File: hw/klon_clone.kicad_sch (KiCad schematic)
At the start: 74 parts

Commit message: Annotated sch.
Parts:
- gave numbers to parts that had none: 70

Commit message: Added all footprints but switch footprint.
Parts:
- C1, C7: footprint (none) -> Capacitor_THT:C_Rect_L13.0mm_W5.0mm_P10.00mm_FKS3_FKP3_MKS4
- C13: footprint (none) -> Capacitor_THT:C_Rect_L10.3mm_W5.0mm_P7.50mm_MKS4
- C14: footprint (none) -> Capacitor_THT:C_Rect_L10.0mm_W4.0mm_P7.50mm_MKS4
- C16, C6: footprint (none) -> Capacitor_THT:CP_Radial_D8.0mm_P5.00mm
- C18: footprint (none) -> Capacitor_THT:C_Rect_L18.0mm_W7.0mm_P15.00mm_FKS3_FKP3
- C19: footprint (none) -> Capacitor_THT:C_Rect_L10.3mm_W4.5mm_P7.50mm_MKS4
- C20: footprint (none) -> Capacitor_THT:C_Rect_L13.0mm_W4.0mm_P10.00mm_FKS3_FKP3_MKS4
- C21: footprint (none) -> Capacitor_THT:C_Rect_L16.5mm_W5.0mm_P15.00mm_MKT
- C22, C5: footprint (none) -> Capacitor_THT:CP_Radial_D5.0mm_P2.00mm
- C3: footprint (none) -> Capacitor_THT:C_Axial_L19.0mm_D9.5mm_P25.00mm_Horizontal
- C4, C9: footprint (none) -> Capacitor_THT:C_Axial_L5.1mm_D3.1mm_P15.00mm_Horizontal
- D4: footprint (none) -> LED_THT:LED_D5.0mm
- D5, D6: footprint (none) -> Diode_THT:D_DO-35_SOD27_P10.16mm_Horizontal
- J1, J3, RV1, RV2, RV3, RV4: footprint (none) -> Connector_PinHeader_2.54mm:PinHeader_1x03_P2.54mm_Vertical
- J2: footprint (none) -> Connector_PinHeader_2.54mm:PinHeader_1x02_P2.54mm_Vertical
- R1, R10, R11, R12, R13, R14, R15, R16, R17, R18, R19, R2, R20, R21, R22, R23, R24, R25, R26, R27, R28, R29, R3, R30, R4, R5, R6, R7, R8, R9: footprint (none) -> Resistor_THT:R_Axial_DIN0207_L6.3mm_D2.5mm_P15.24mm_Horizontal
- SW1, SW2: footprint (none) -> Connector_PinHeader_2.54mm:PinHeader_1x06_P2.54mm_Vertical

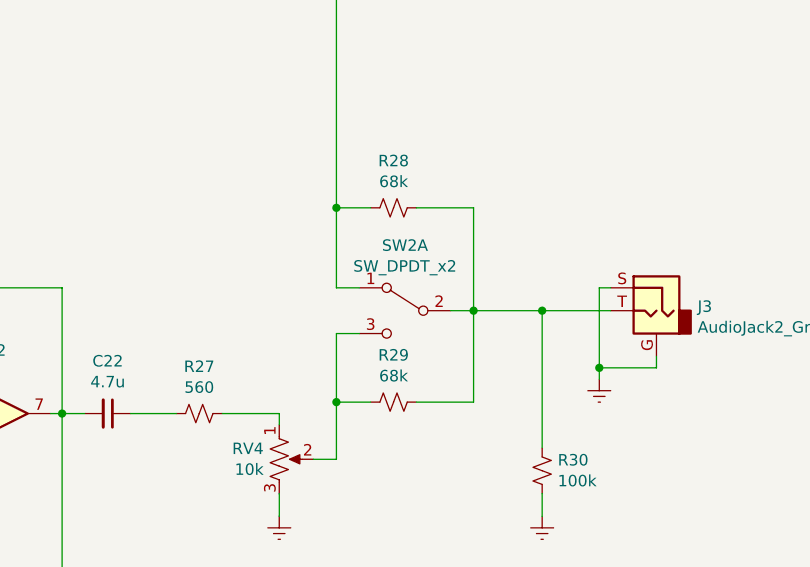
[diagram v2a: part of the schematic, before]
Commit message: Added SOIC Opamp footprints.
Added tenative footprints for opamps. Double check we have right package. Need to add footprint for Power supply IC>
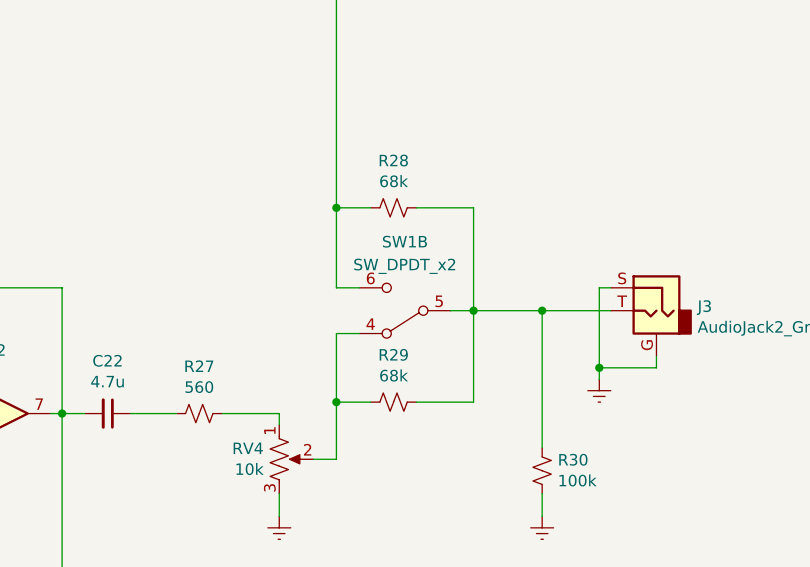
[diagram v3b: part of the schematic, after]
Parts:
- removed SW2: SW_DPDT_x2, Connector_PinHeader_2.54mm:PinHeader_1x06_P2.54mm_Vertical, symbol Switch:SW_DPDT_x2
- added unit 2 of SW1
- U1, U3: footprint (none) -> Package_SO:SO-8_5.3x6.2mm_P1.27mm
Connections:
- net at R29.2, RV4.2: now also SW1.4 (A)
- net at R28.2, R7.1: now also SW1.6 (C)
- net at J3.T, R28.1, R29.1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: now also SW1.5 (B)
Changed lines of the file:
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@@
     (property "Reference" "U1" (id 0) (at 87.63 71.9582 0))
     (property "Value" "TL072" (id 1) (at 87.63 74.2696 0))
-    (property "Footprint" "" (id 2) (at 87.63 81.28 0)
+    (property "Footprint" "Package_SO:SO-8_5.3x6.2mm_P1.27mm" (id 2) (at 87.63 81.28 0)
       (effects (font (size 1.27 1.27)) hide)
     )
@@
     (property "Reference" "U1" (id 0) (at 173.99 74.4982 0))
     (property "Value" "TL072" (id 1) (at 173.99 76.8096 0))
-    (property "Footprint" "" (id 2) (at 173.99 83.82 0)
+    (property "Footprint" "Package_SO:SO-8_5.3x6.2mm_P1.27mm" (id 2) (at 173.99 83.82 0)
       (effects (font (size 1.27 1.27)) hide)
     )
@@
     (property "Reference" "U3" (id 0) (at 279.4 77.0382 0))
     (property "Value" "TL072" (id 1) (at 279.4 79.3496 0))
-    (property "Footprint" "" (id 2) (at 279.4 86.36 0)
+    (property "Footprint" "Package_SO:SO-8_5.3x6.2mm_P1.27mm" (id 2) (at 279.4 86.36 0)
       (effects (font (size 1.27 1.27)) hide)
     )
@@
     (property "Reference" "U3" (id 0) (at 318.77 79.5782 0))
     (property "Value" "TL072" (id 1) (at 318.77 81.8896 0))
-    (property "Footprint" "" (id 2) (at 318.77 88.9 0)
+    (property "Footprint" "Package_SO:SO-8_5.3x6.2mm_P1.27mm" (id 2) (at 318.77 88.9 0)
       (effects (font (size 1.27 1.27)) hide)
     )
@@
     )
     (property "Datasheet" "~" (id 3) (at 351.79 93.98 0)
-      (effects (font (size 1.27 1.27)) hide)
-    )
-    (pin "1")
-    (pin "2")
-    (pin "3")
-  )
-  (symbol (lib_id "Switch:SW_DPDT_x2") (at 365.76 77.47 0) (mirror y) (unit 1)
-    (in_bom yes) (on_board yes)
-    (property "Reference" "SW2" (id 0) (at 365.76 70.231 0))
-    (property "Value" "SW_DPDT_x2" (id 1) (at 365.76 72.5424 0))
-    (property "Footprint" "Connector_PinHeader_2.54mm:PinHeader_1x06_P2.54mm_Vertical" (id 2) (at 365.76 77.47 0)
-      (effects (font (size 1.27 1.27)) hide)
-    )
-    (property "Datasheet" "~" (id 3) (at 365.76 77.47 0)
       (effects (font (size 1.27 1.27)) hide)
     )
@@
       (effects (font (size 1.27 1.27)) (justify left))
     )
-    (property "Footprint" "" (id 2) (at 87.63 81.28 0)
+    (property "Footprint" "Package_SO:SO-8_5.3x6.2mm_P1.27mm" (id 2) (at 87.63 81.28 0)
       (effects (font (size 1.27 1.27)) hide)
     )
@@
       (effects (font (size 1.27 1.27)) (justify left))
     )
-    (property "Footprint" "" (id 2) (at 279.4 86.36 0)
+    (property "Footprint" "Package_SO:SO-8_5.3x6.2mm_P1.27mm" (id 2) (at 279.4 86.36 0)
       (effects (font (size 1.27 1.27)) hide)
     )
@@
     )
     (pin "1")
+  )
+  (symbol (lib_id "Switch:SW_DPDT_x2") (at 365.76 77.47 180) (unit 2)
+    (in_bom yes) (on_board yes) (fields_autoplaced)
+    (property "Reference" "SW1" (id 0) (at 365.76 69.85 0))
+    (property "Value" "SW_DPDT_x2" (id 1) (at 365.76 72.39 0))
+    (property "Footprint" "Connector_PinHeader_2.54mm:PinHeader_1x06_P2.54mm_Vertical" (id 2) (at 365.76 77.47 0)
+      (effects (font (size 1.27 1.27)) hide)
+    )
+    (property "Datasheet" "~" (id 3) (at 365.76 77.47 0)
+      (effects (font (size 1.27 1.27)) hide)
+    )
+    (pin "4")
+    (pin "5")
+    (pin "6")
   )
   (sheet_instances
@@
       (reference "SW1") (unit 1) (value "SW_DPDT_x2") (footprint "Connector_PinHeader_2.54mm:PinHeader_1x06_P2.54mm_Vertical")
     )
-    (path "/00000000-0000-0000-0000-000061c3b78a"
-      (reference "SW2") (unit 1) (value "SW_DPDT_x2") (footprint "Connector_PinHeader_2.54mm:PinHeader_1x06_P2.54mm_Vertical")
+    (path "/a1c80773-df7f-4f73-ae79-2de08d81dd4b"
+      (reference "SW1") (unit 2) (value "SW_DPDT_x2") (footprint "Connector_PinHeader_2.54mm:PinHeader_1x06_P2.54mm_Vertical")
     )
     (path "/00000000-0000-0000-0000-000061c0f078"
-      (reference "U1") (unit 1) (value "TL072") (footprint "")
+      (reference "U1") (unit 1) (value "TL072") (footprint "Package_SO:SO-8_5.3x6.2mm_P1.27mm")
     )
     (path "/00000000-0000-0000-0000-000061c176e6"
-      (reference "U1") (unit 2) (value "TL072") (footprint "")
+      (reference "U1") (unit 2) (value "TL072") (footprint "Package_SO:SO-8_5.3x6.2mm_P1.27mm")
     )
     (path "/00000000-0000-0000-0000-000061c5b223"
-      (reference "U1") (unit 3) (value "TL072") (footprint "")
+      (reference "U1") (unit 3) (value "TL072") (footprint "Package_SO:SO-8_5.3x6.2mm_P1.27mm")
     )
     (path "/00000000-0000-0000-0000-000061c4201c"
@@
     )
     (path "/00000000-0000-0000-0000-000061c29fb1"
-      (reference "U3") (unit 1) (value "TL072") (footprint "")
+      (reference "U3") (unit 1) (value "TL072") (footprint "Package_SO:SO-8_5.3x6.2mm_P1.27mm")
     )
     (path "/00000000-0000-0000-0000-000061c35021"
-      (reference "U3") (unit 2) (value "TL072") (footprint "")
+      (reference "U3") (unit 2) (value "TL072") (footprint "Package_SO:SO-8_5.3x6.2mm_P1.27mm")
     )
     (path "/00000000-0000-0000-0000-000061c5fbc0"
-      (reference "U3") (unit 3) (value "TL072") (footprint "")
-    )
-  )
+      (reference "U3") (unit 3) (value "TL072") (footprint "Package_SO:SO-8_5.3x6.2mm_P1.27mm")
+    )
+  )

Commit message: Assigned SO8 to ICL7660
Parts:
- U2: footprint (none) -> Package_SO:SO-8_5.3x6.2mm_P1.27mm
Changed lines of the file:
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@@
     (property "Reference" "U2" (id 0) (at 168.91 192.6082 0))
     (property "Value" "ICL7660" (id 1) (at 168.91 194.9196 0))
-    (property "Footprint" "" (id 2) (at 166.37 209.55 0)
+    (property "Footprint" "Package_SO:SO-8_5.3x6.2mm_P1.27mm" (id 2) (at 166.37 209.55 0)
       (effects (font (size 1.27 1.27)) hide)
     )
@@
     )
     (path "/00000000-0000-0000-0000-000061c4201c"
-      (reference "U2") (unit 1) (value "ICL7660") (footprint "")
+      (reference "U2") (unit 1) (value "ICL7660") (footprint "Package_SO:SO-8_5.3x6.2mm_P1.27mm")
     )
     (path "/00000000-0000-0000-0000-000061c29fb1"

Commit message: Assigned new cap footprint for 1uF
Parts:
- C10, C11, C12, C15, C17, C2, C8: footprint (none) -> kicad_footprint_library:C_Axial_L17.5mm_W7.8mm_P7.5mm_Horizontal
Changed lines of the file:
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@@
     (property "Reference" "C15" (id 0) (at 189.23 78.0034 90))
     (property "Value" "1u" (id 1) (at 189.23 80.3148 90))
-    (property "Footprint" "" (id 2) (at 189.23 83.82 0)
+    (property "Footprint" "kicad_footprint_library:C_Axial_L17.5mm_W7.8mm_P7.5mm_Horizontal" (id 2) (at 189.23 83.82 0)
       (effects (font (size 1.27 1.27)) hide)
     )
@@
       (effects (font (size 1.27 1.27)) (justify left))
     )
-    (property "Footprint" "" (id 2) (at 147.32 57.15 0)
+    (property "Footprint" "kicad_footprint_library:C_Axial_L17.5mm_W7.8mm_P7.5mm_Horizontal" (id 2) (at 147.32 57.15 0)
       (effects (font (size 1.27 1.27)) hide)
     )
@@
     (property "Reference" "C17" (id 0) (at 224.79 78.0034 90))
     (property "Value" "1u" (id 1) (at 224.79 80.3148 90))
-    (property "Footprint" "" (id 2) (at 224.79 83.82 0)
+    (property "Footprint" "kicad_footprint_library:C_Axial_L17.5mm_W7.8mm_P7.5mm_Horizontal" (id 2) (at 224.79 83.82 0)
       (effects (font (size 1.27 1.27)) hide)
     )
@@
       (effects (font (size 1.27 1.27)) (justify left))
     )
-    (property "Footprint" "" (id 2) (at 153.67 209.55 0)
+    (property "Footprint" "kicad_footprint_library:C_Axial_L17.5mm_W7.8mm_P7.5mm_Horizontal" (id 2) (at 153.67 209.55 0)
       (effects (font (size 1.27 1.27)) hide)
     )
@@
       (effects (font (size 1.27 1.27)) (justify left))
     )
-    (property "Footprint" "" (id 2) (at 110.49 205.74 0)
+    (property "Footprint" "kicad_footprint_library:C_Axial_L17.5mm_W7.8mm_P7.5mm_Horizontal" (id 2) (at 110.49 205.74 0)
       (effects (font (size 1.27 1.27)) hide)
     )
@@
       (effects (font (size 1.27 1.27)) (justify left))
     )
-    (property "Footprint" "" (id 2) (at 143.51 209.55 0)
+    (property "Footprint" "kicad_footprint_library:C_Axial_L17.5mm_W7.8mm_P7.5mm_Horizontal" (id 2) (at 143.51 209.55 0)
       (effects (font (size 1.27 1.27)) hide)
     )
@@
     (property "Reference" "C8" (id 0) (at 130.81 198.6534 90))
     (property "Value" "1u" (id 1) (at 130.81 200.9648 90))
-    (property "Footprint" "" (id 2) (at 130.81 204.47 0)
+    (property "Footprint" "kicad_footprint_library:C_Axial_L17.5mm_W7.8mm_P7.5mm_Horizontal" (id 2) (at 130.81 204.47 0)
       (effects (font (size 1.27 1.27)) hide)
     )
@@
     )
     (path "/00000000-0000-0000-0000-000061c48bfa"
-      (reference "C2") (unit 1) (value "1u") (footprint "")
+      (reference "C2") (unit 1) (value "1u") (footprint "kicad_footprint_library:C_Axial_L17.5mm_W7.8mm_P7.5mm_Horizontal")
     )
     (path "/00000000-0000-0000-0000-000061c22f5d"
@@
     )
     (path "/00000000-0000-0000-0000-000061c4d822"
-      (reference "C8") (unit 1) (value "1u") (footprint "")
+      (reference "C8") (unit 1) (value "1u") (footprint "kicad_footprint_library:C_Axial_L17.5mm_W7.8mm_P7.5mm_Horizontal")
     )
     (path "/00000000-0000-0000-0000-000061c1630a"
@@
     )
     (path "/00000000-0000-0000-0000-000061c4c2d3"
-      (reference "C10") (unit 1) (value "1u") (footprint "")
+      (reference "C10") (unit 1) (value "1u") (footprint "kicad_footprint_library:C_Axial_L17.5mm_W7.8mm_P7.5mm_Horizontal")
     )
     (path "/00000000-0000-0000-0000-000061c1ce7f"
-      (reference "C11") (unit 1) (value "1u") (footprint "")
+      (reference "C11") (unit 1) (value "1u") (footprint "kicad_footprint_library:C_Axial_L17.5mm_W7.8mm_P7.5mm_Horizontal")
     )
     (path "/00000000-0000-0000-0000-000061c46c41"
-      (reference "C12") (unit 1) (value "1u") (footprint "")
+      (reference "C12") (unit 1) (value "1u") (footprint "kicad_footprint_library:C_Axial_L17.5mm_W7.8mm_P7.5mm_Horizontal")
     )
     (path "/00000000-0000-0000-0000-000061c1b7dc"
@@
     )
     (path "/00000000-0000-0000-0000-000061c1c148"
-      (reference "C15") (unit 1) (value "1u") (footprint "")
+      (reference "C15") (unit 1) (value "1u") (footprint "kicad_footprint_library:C_Axial_L17.5mm_W7.8mm_P7.5mm_Horizontal")
     )
     (path "/00000000-0000-0000-0000-000061c4d184"
@@
     )
     (path "/00000000-0000-0000-0000-000061c21611"
-      (reference "C17") (unit 1) (value "1u") (footprint "")
+      (reference "C17") (unit 1) (value "1u") (footprint "kicad_footprint_library:C_Axial_L17.5mm_W7.8mm_P7.5mm_Horizontal")
     )
     (path "/00000000-0000-0000-0000-000061c2197d"

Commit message: Updated J1/J3 footprints and symbols. Initial layout placement.
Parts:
- removed J1, J3: AudioJack2_Ground, Connector_PinHeader_2.54mm:PinHeader_1x03_P2.54mm_Vertical, symbol Connector:AudioJack2_Ground
- added J1, J3: Conn_01x03_Male, Connector_PinHeader_2.54mm:PinHeader_1x03_P2.54mm_Vertical, symbol Connector:Conn_01x03_Male
- C10, C12, C2, C8: footprint kicad_footprint_library:C_Axial_L17.5mm_W7.8mm_P7.5mm_Horizontal -> Capacitor_SMD:C_0805_2012Metric_Pad1.18x1.45mm_HandSolder
- R1, R10, R11, R12, R13, R14, R15, R16, R17, R18, R19, R2, R20, R21, R22, R23, R24, R25, R26, R27, R28, R29, R3, R30, R4, R5, R6, R7, R8, R9: footprint Resistor_THT:R_Axial_DIN0207_L6.3mm_D2.5mm_P15.24mm_Horizontal -> Resistor_SMD:R_0805_2012Metric_Pad1.20x1.40mm_HandSolder
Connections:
- net Earth: now also J1.2 (Pin_2), J1.3 (Pin_3), J3.2 (Pin_2), J3.3 (Pin_3)
- net at R1.2: now also J1.1 (Pin_1)
- net at R28.1, R29.1, R30.1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: now also J3.1 (Pin_1)

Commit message: PCB Updates
Almost completed board. FInished traces, poured GND plane on layer2, added names and mounting holes.
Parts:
- added J4, J5, J6, J7: Conn_01x01_Female, MountingHole:MountingHole_3.2mm_M3, symbol Connector:Conn_01x01_Female
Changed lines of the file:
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@@
+    (pin "1")
+  )
+  (symbol (lib_id "Connector:Conn_01x01_Female") (at 29.21 143.51 0) (unit 1)
+    (in_bom yes) (on_board yes) (fields_autoplaced)
+    (property "Reference" "J6" (id 0) (at 30.48 142.2399 0)
+      (effects (font (size 1.27 1.27)) (justify left))
+    )
+    (property "Value" "Conn_01x01_Female" (id 1) (at 30.48 144.7799 0)
+      (effects (font (size 1.27 1.27)) (justify left))
+    )
+    (property "Footprint" "MountingHole:MountingHole_3.2mm_M3" (id 2) (at 29.21 143.51 0)
+      (effects (font (size 1.27 1.27)) hide)
+    )
+    (property "Datasheet" "~" (id 3) (at 29.21 143.51 0)
+      (effects (font (size 1.27 1.27)) hide)
+    )
+    (pin "1")
+  )
+  (symbol (lib_id "Connector:Conn_01x01_Female") (at 29.21 149.86 0) (unit 1)
+    (in_bom yes) (on_board yes) (fields_autoplaced)
+    (property "Reference" "J7" (id 0) (at 30.48 148.5899 0)
+      (effects (font (size 1.27 1.27)) (justify left))
+    )
+    (property "Value" "Conn_01x01_Female" (id 1) (at 30.48 151.1299 0)
+      (effects (font (size 1.27 1.27)) (justify left))
+    )
+    (property "Footprint" "MountingHole:MountingHole_3.2mm_M3" (id 2) (at 29.21 149.86 0)
+      (effects (font (size 1.27 1.27)) hide)
+    )
+    (property "Datasheet" "~" (id 3) (at 29.21 149.86 0)
+      (effects (font (size 1.27 1.27)) hide)
+    )
+    (pin "1")
+  )
+  (symbol (lib_id "Connector:Conn_01x01_Female") (at 29.21 137.16 0) (unit 1)
+    (in_bom yes) (on_board yes) (fields_autoplaced)
+    (property "Reference" "J5" (id 0) (at 30.48 135.8899 0)
+      (effects (font (size 1.27 1.27)) (justify left))
+    )
+    (property "Value" "Conn_01x01_Female" (id 1) (at 30.48 138.4299 0)
+      (effects (font (size 1.27 1.27)) (justify left))
+    )
+    (property "Footprint" "MountingHole:MountingHole_3.2mm_M3" (id 2) (at 29.21 137.16 0)
+      (effects (font (size 1.27 1.27)) hide)
+    )
+    (property "Datasheet" "~" (id 3) (at 29.21 137.16 0)
+      (effects (font (size 1.27 1.27)) hide)
+    )
     (pin "1")
   )
@@
     (pin "3")
   )
+  (symbol (lib_id "Connector:Conn_01x01_Female") (at 29.21 130.81 0) (unit 1)
+    (in_bom yes) (on_board yes) (fields_autoplaced)
+    (property "Reference" "J4" (id 0) (at 30.48 129.5399 0)
+      (effects (font (size 1.27 1.27)) (justify left))
+    )
+    (property "Value" "Conn_01x01_Female" (id 1) (at 30.48 132.0799 0)
+      (effects (font (size 1.27 1.27)) (justify left))
+    )
+    (property "Footprint" "MountingHole:MountingHole_3.2mm_M3" (id 2) (at 29.21 130.81 0)
+      (effects (font (size 1.27 1.27)) hide)
+    )
+    (property "Datasheet" "~" (id 3) (at 29.21 130.81 0)
+      (effects (font (size 1.27 1.27)) hide)
+    )
+    (pin "1")
+  )
   (symbol (lib_id "Connector:Conn_01x03_Male") (at 20.32 81.28 0) (unit 1)
     (in_bom yes) (on_board yes) (fields_autoplaced)
@@
       (reference "J3") (unit 1) (value "Conn_01x03_Male") (footprint "Connector_PinHeader_2.54mm:PinHeader_1x03_P2.54mm_Vertical")
     )
+    (path "/f4e1b81e-f02a-451a-905f-f000b6b75e92"
+      (reference "J4") (unit 1) (value "Conn_01x01_Female") (footprint "MountingHole:MountingHole_3.2mm_M3")
+    )
+    (path "/43a76f37-3a32-4717-8fc4-a788fd3aa15a"
+      (reference "J5") (unit 1) (value "Conn_01x01_Female") (footprint "MountingHole:MountingHole_3.2mm_M3")
+    )
+    (path "/08dc2e7f-ea05-46c4-80ea-0bae1d02c857"
+      (reference "J6") (unit 1) (value "Conn_01x01_Female") (footprint "MountingHole:MountingHole_3.2mm_M3")
+    )
+    (path "/375d2241-2727-41a2-b2ae-e7a2f896177b"
+      (reference "J7") (unit 1) (value "Conn_01x01_Female") (footprint "MountingHole:MountingHole_3.2mm_M3")
+    )
     (path "/00000000-0000-0000-0000-000061c0da92"
